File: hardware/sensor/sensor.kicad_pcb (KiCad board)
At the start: 2 copper layers, 100 x 100 mm, 70 parts, among them J1 Conn_01x02_Female, J2 Conn_01x06_Female, Q1 Q_PMOS_DGS, Q2 Q_NMOS_DGS, U1 L5973D, U2 L5973D, U3 ATSAMD21G18A-A, U4 BME280, U5 AT24CS04-STUM, U6 ATECC608A-SSHDA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

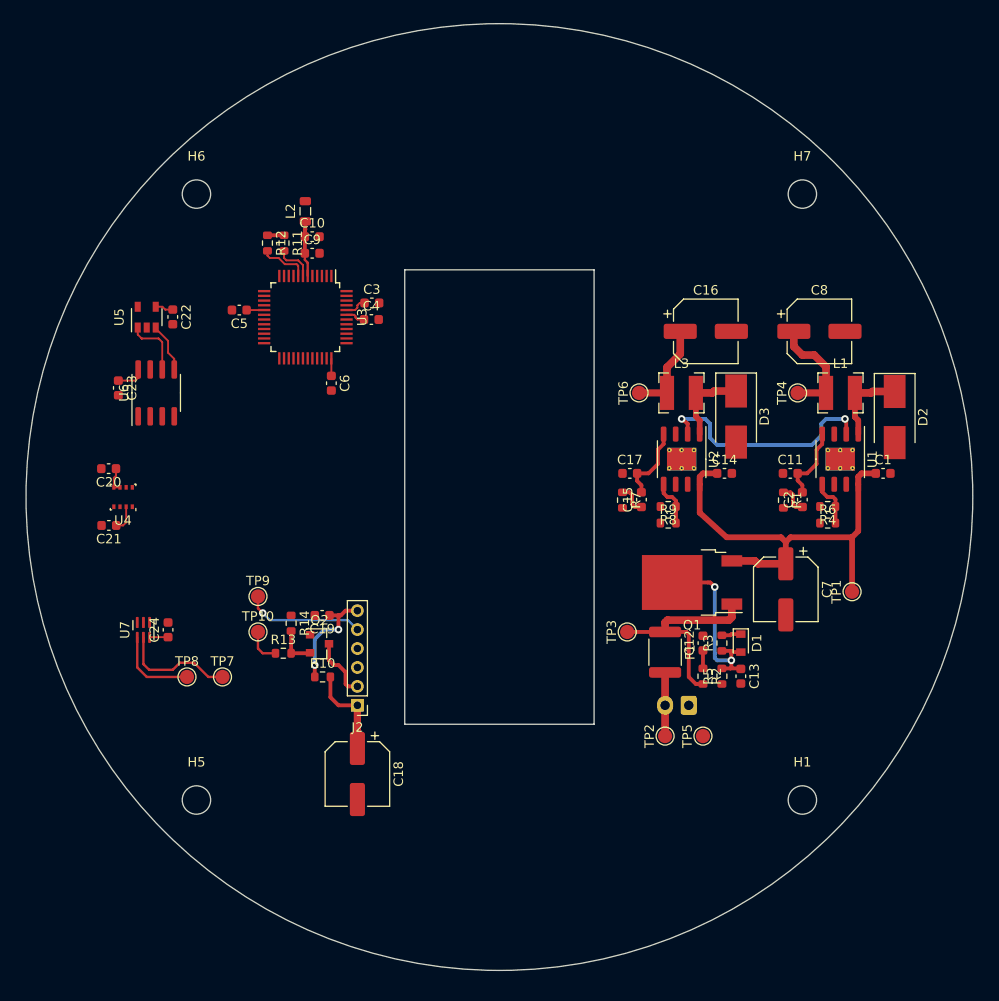
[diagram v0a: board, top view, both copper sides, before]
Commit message: Initial layout is complete
Removes mounting points as they're present in the DXF
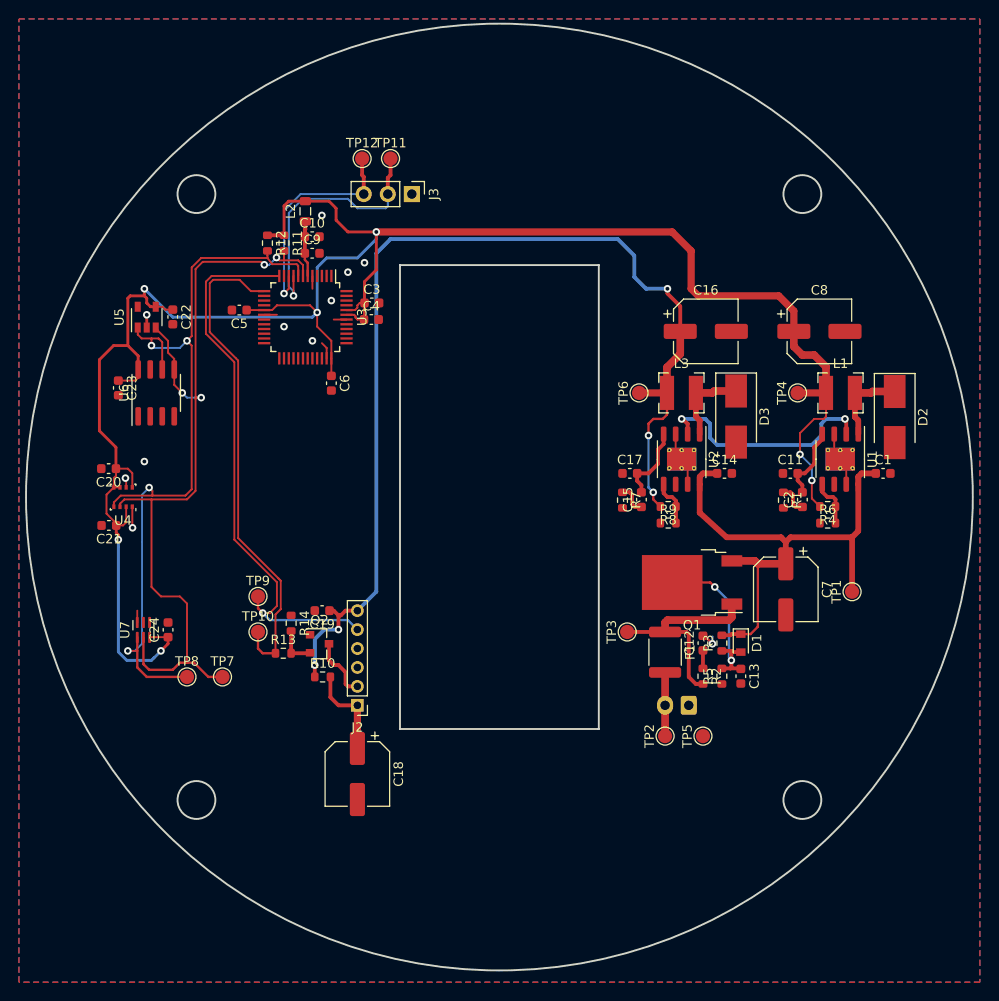
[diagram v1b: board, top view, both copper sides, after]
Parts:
- removed H1, H5, H6, H7: MountingHole, MountingHole:MountingHole_3mm
- added J3: Conn_01x03_Male, Connector_PinHeader_2.54mm:PinHeader_1x03_P2.54mm_Vertical, F.Cu at (-9.25, -32.0)
- added TP11: TestPoint_Flag, TestPoint:TestPoint_Pad_D1.5mm, F.Cu at (-11.5, -35.8)
- added TP12: TestPoint_Flag, TestPoint:TestPoint_Pad_D1.5mm, F.Cu at (-14.5, -35.8)
- moved C19 0.50 mm to (-18.7, 12.0)
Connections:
- U3 pad 10: Net-(U3-Pad10) -> /N302
- U3 pad 9: Net-(U3-Pad9) -> /N301
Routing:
- net +3V3: track 34.1 -> 227.1 mm, vias 0 -> 7
- net +5V: track 21.6 -> 114.2 mm, vias 2 -> 5
- net /I2C_SDA: track 21.8 -> 90.1 mm, vias 0 -> 4
- net /I2C_SCL: track 20.7 -> 87.9 mm, vias 0 -> 4
- net /N205: track 3.81 -> 52.6 mm
- net /N203: track 12.7 -> 59.8 mm
- net /N301: track 0.00 -> 27.8 mm, vias 0 -> 1
- net GND: track 0.00 -> 25.5 mm, vias 0 -> 11
- net /N302: track 0.00 -> 23.8 mm, vias 0 -> 1
- net /N104: track 47.9 -> 56.7 mm
- net /N105: track 19.9 -> 19.1 mm
- added copper zone on B.Cu, net GND
- added copper zone on F.Cu, net GND
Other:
- outline, holes or cut-outs redrawn

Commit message: Fixes power input clearance
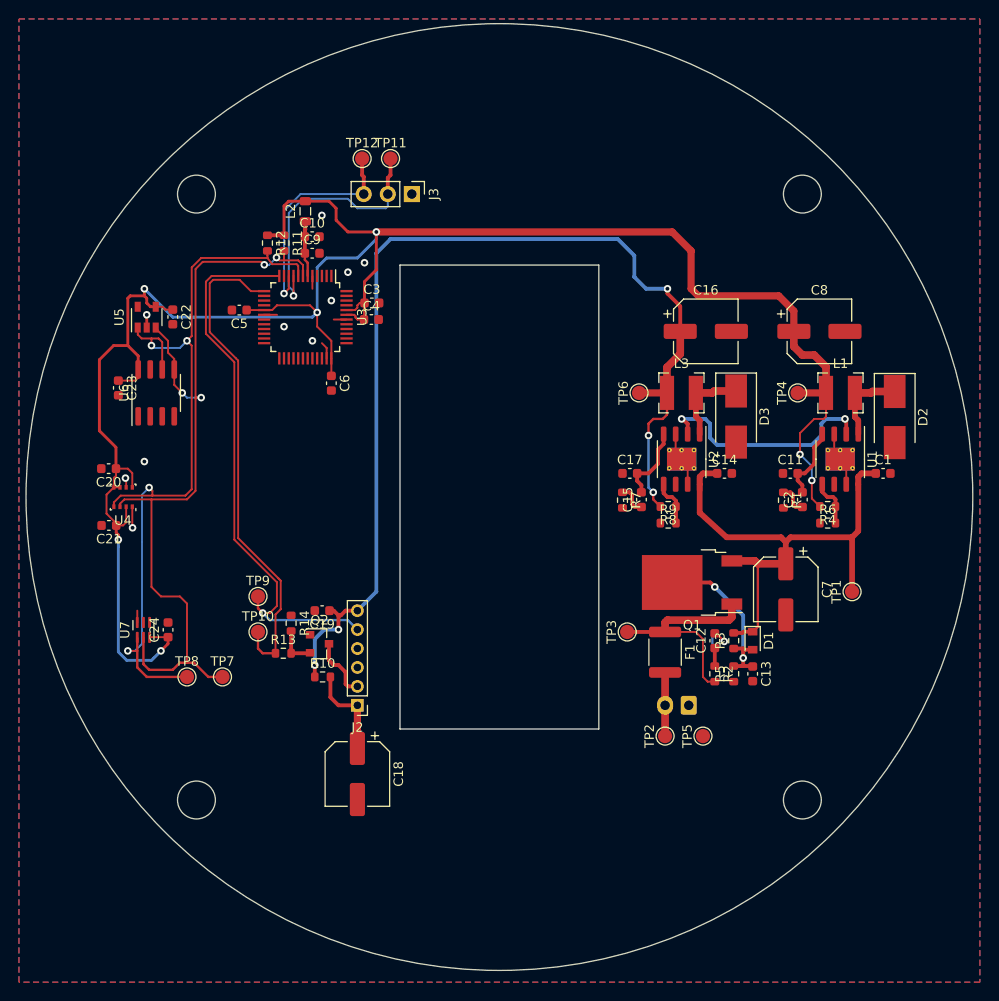
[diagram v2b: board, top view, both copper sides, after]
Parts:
- moved C12 1.27 mm to (22.8, 15.2)
- moved C13 1.27 mm to (26.8, 18.7)
- moved D1 1.27 mm to (26.8, 15.2)
- moved R2 1.27 mm to (22.8, 18.7)
- moved R3 1.27 mm to (24.8, 15.2)
- moved R5 1.27 mm to (24.8, 18.7)
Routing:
- net /N104: track 56.7 -> 55.7 mm
- net /N102: track 22.6 -> 23.4 mm
